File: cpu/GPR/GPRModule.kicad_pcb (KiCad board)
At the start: 2 copper layers, 100 x 80 mm, 50 parts, among them J1 Interconnect, U1 74HCT574, U10 74LS245, U11 74LS126, U2 74HCT574, U3 74LS245, U4 74LS245, U5 74LS245, U6 74LS245, U7 74LS245, U8 74LS245, U9 74LS245

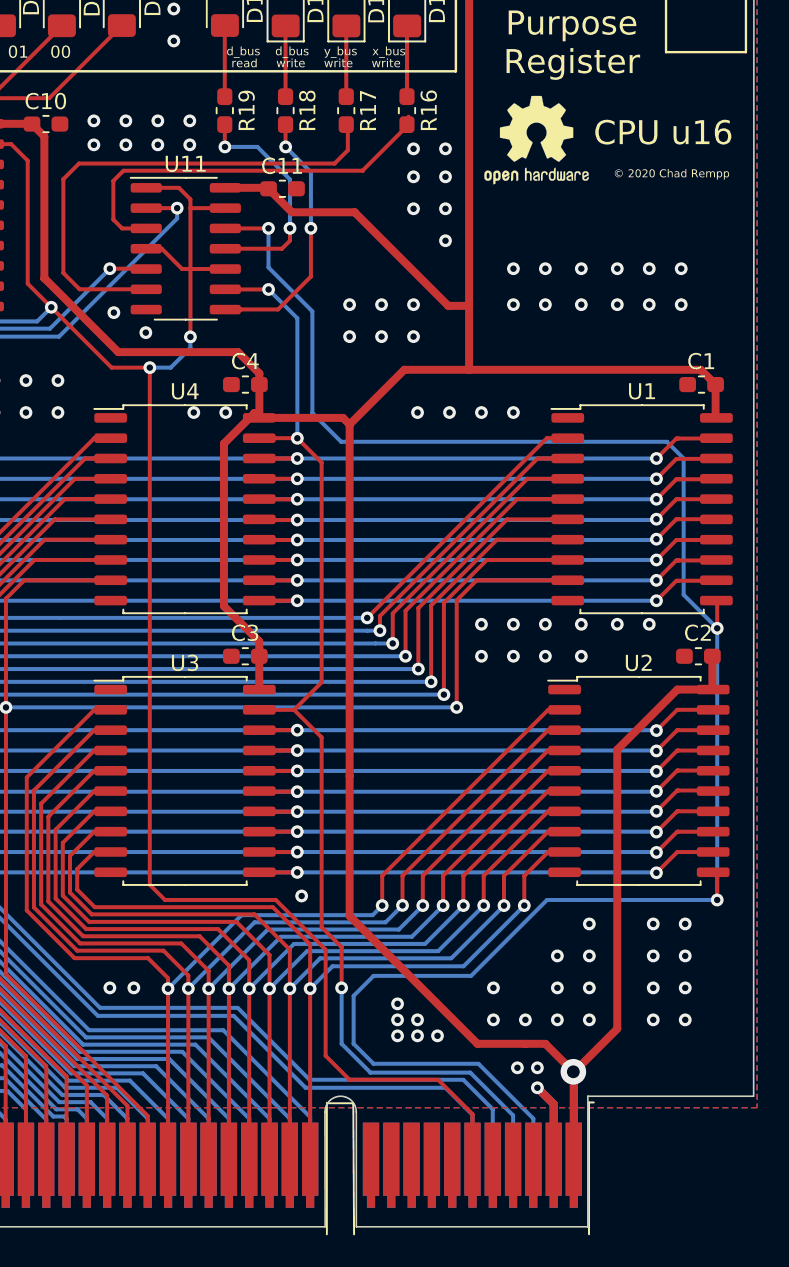
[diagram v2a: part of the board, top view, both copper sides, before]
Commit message: Added missing power pins to GPR
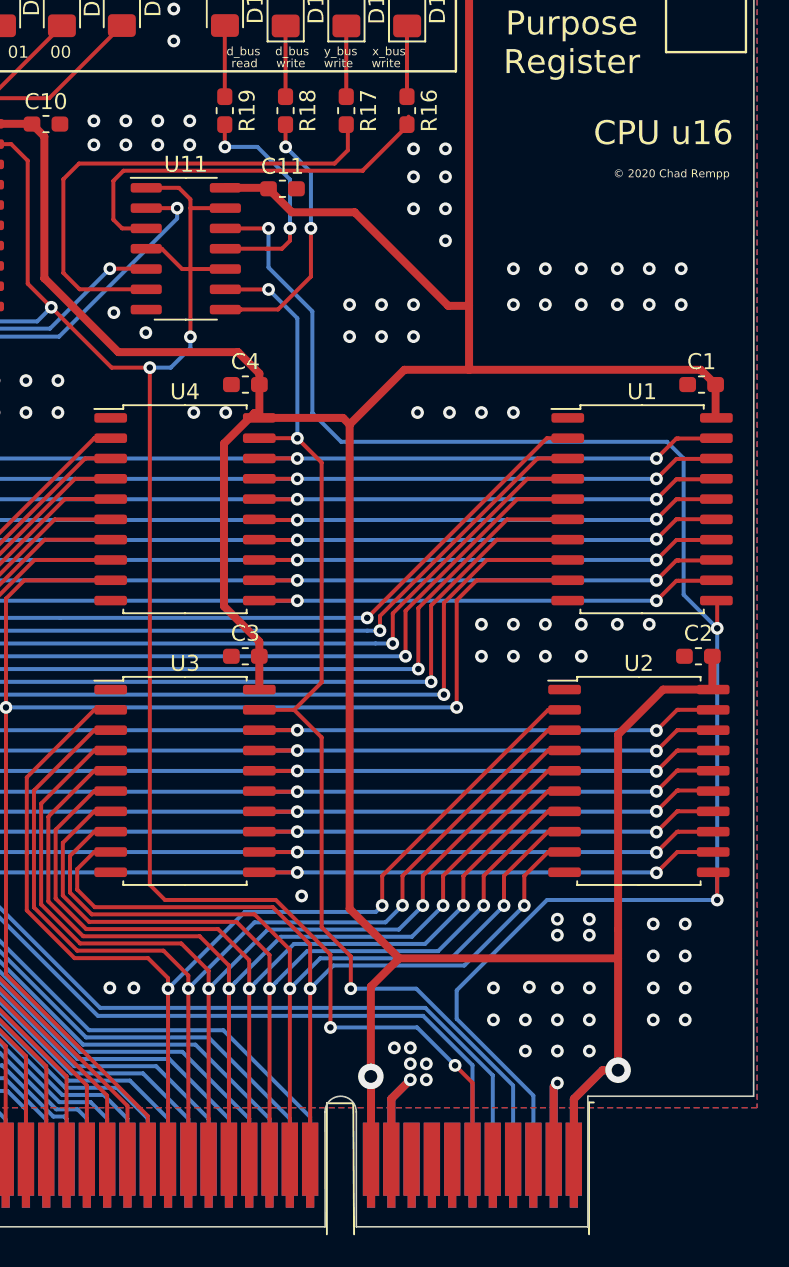
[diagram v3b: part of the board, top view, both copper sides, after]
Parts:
- removed REF**: OSHW, Symbol:OSHW-Logo2_7.3x6mm_SilkScreen
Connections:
- J1 pad A52: Net-(J1-PadA52) -> +5V
- J1 pad A53: Net-(J1-PadA53) -> GND
- J1 pad B52: Net-(J1-PadB52) -> +5V
- J1 pad B53: Net-(J1-PadB53) -> GND
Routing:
- net +5V: track 357.6 -> 383.9 mm, vias 1 -> 2
- net GND: track 15.1 -> 31.3 mm, vias 185 -> 188
- net /d_bus_read: track 118.9 -> 106.1 mm
- net Net-(J1-PadB53): track 2.66 -> 0.00 mm
- net Net-(J1-PadB52): track 2.66 -> 0.00 mm
- net Net-(J1-PadA53): track 2.66 -> 0.00 mm
- net Net-(J1-PadA52): track 2.66 -> 0.00 mm
- net /~y_bus_write: track 166.9 -> 168.7 mm
- net /~d_bus_write: track 75.8 -> 74.5 mm
- net /~x_bus_write: track 117.1 -> 118.3 mm
- net /~DBG: track 154.4 -> 154.3 mm, vias 4 -> 6

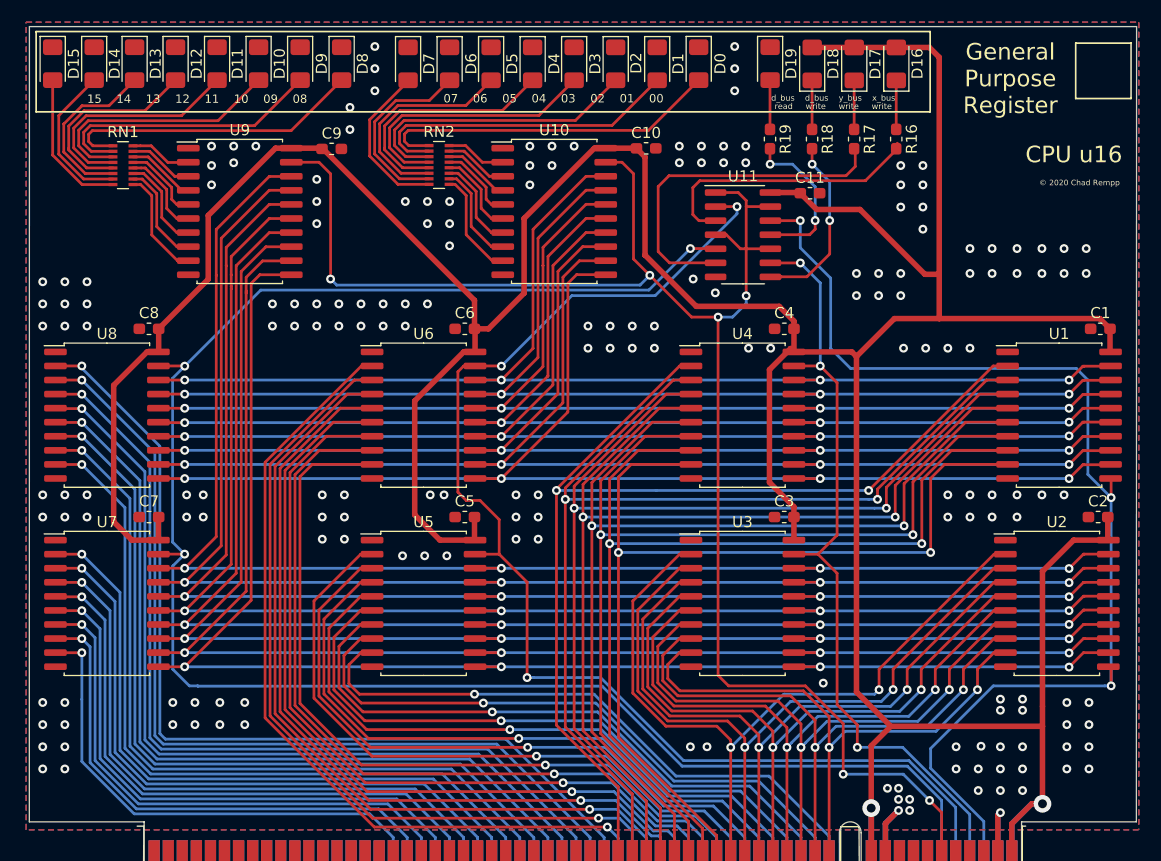
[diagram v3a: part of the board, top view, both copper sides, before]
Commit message: Added 10uF caps to GPR
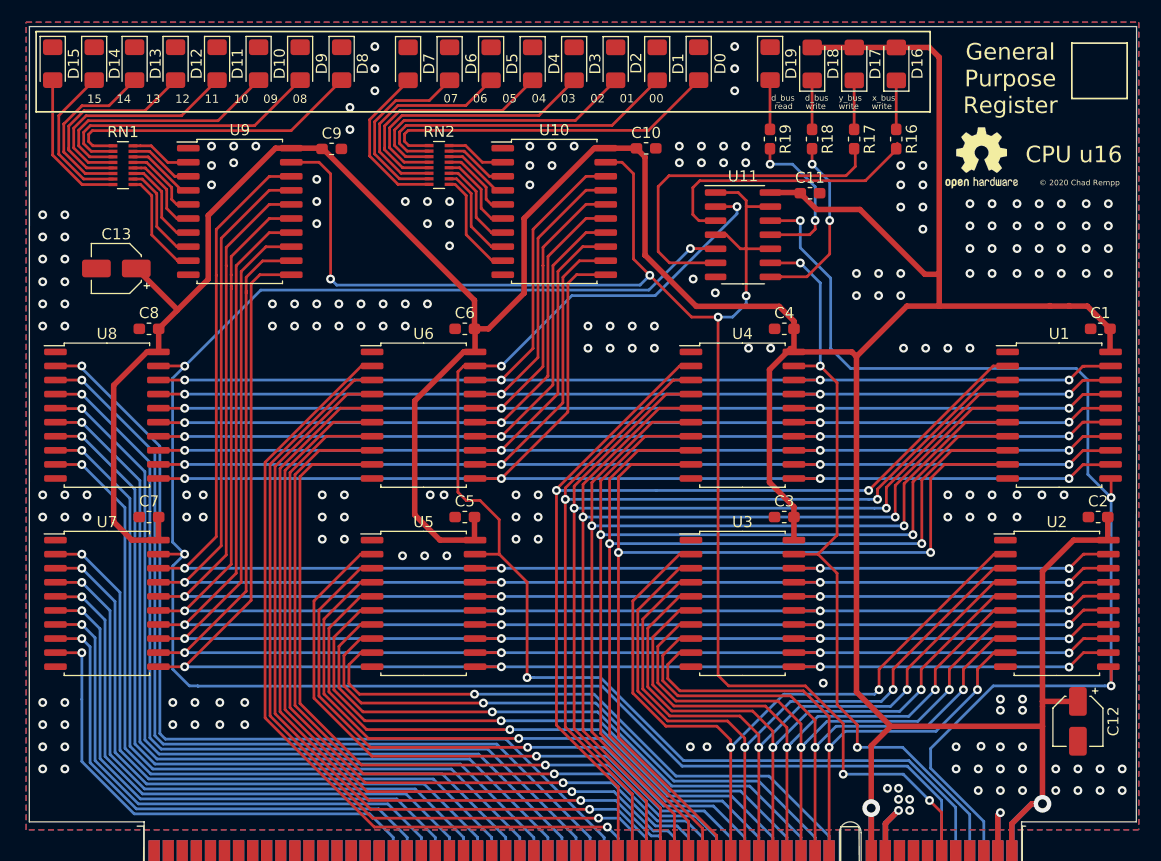
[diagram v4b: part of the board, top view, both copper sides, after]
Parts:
- added C12: 10uF, Capacitor_SMD:CP_Elec_4x5.4, F.Cu at (186.5, 120.2)
- added C13: 10uF, Capacitor_SMD:CP_Elec_4x5.4, F.Cu at (99.7, 79.3)
- added REF**: OSHW-Logo2_7.3x6mm_SilkScreen, Symbol:OSHW-Logo2_7.3x6mm_SilkScreen, F.Cu at (177.8, 69.3)
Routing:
- net +5V: track 383.9 -> 392.3 mm
- net GND: vias 188 -> 207
